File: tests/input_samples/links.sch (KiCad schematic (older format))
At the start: 4 parts, among them J1 Molex KK, J2 Molex KK

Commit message: Added `datasheet_as_link` example.
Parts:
- C1: manf# (none) -> C0805C102K5RACTU
- J1, J2: manf# (none) -> 0022232021
- R1: manf# (none) -> CR0805-JW-102ELF
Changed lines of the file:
@@
 F 3 "https://www.molex.com/webdocs/datasheets/pdf/en-us//0022232021_PCB_HEADERS.pdf" H 2850 2300 50  0001 C CNN
 F 4 "900-0022232021-ND" H 2850 2300 50  0001 C CNN "digikey#"
+F 5 "0022232021" H 2850 2300 50  0001 C CNN "manf#"
 	1    2850 2300
 	1    0    0    -1
@@
 F 3 "https://www.molex.com/webdocs/datasheets/pdf/en-us//0022232021_PCB_HEADERS.pdf" H 4500 2300 50  0001 C CNN
 F 4 "900-0022232021-ND" H 4500 2300 50  0001 C CNN "digikey#"
+F 5 "0022232021" H 4500 2300 50  0001 C CNN "manf#"
 	1    4500 2300
 	-1   0    0    -1
@@
 F 3 "https://www.bourns.com/docs/product-datasheets/CRxxxxx.pdf" H 3450 2300 50  0001 C CNN
 F 4 "CR0805-JW-102ELFCT-ND" V 3450 2300 50  0001 C CNN "digikey#"
+F 5 "CR0805-JW-102ELF" V 3450 2300 50  0001 C CNN "manf#"
 	1    3450 2300
 	0    1    1    0
@@
 F 3 "https://content.kemet.com/datasheets/KEM_C1002_X7R_SMD.pdf" H 3750 2500 50  0001 C CNN
 F 4 "399-1147-1-ND" H 3750 2500 50  0001 C CNN "digikey#"
+F 5 "C0805C102K5RACTU" H 3750 2500 50  0001 C CNN "manf#"
 	1    3750 2500
 	1    0    0    -1

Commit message: Added test for data_sheet_as_link in the DNF section.
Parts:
- C1: Config (none) -> DNF
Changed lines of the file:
@@
 F 4 "399-1147-1-ND" H 3750 2500 50  0001 C CNN "digikey#"
 F 5 "C0805C102K5RACTU" H 3750 2500 50  0001 C CNN "manf#"
+F 6 "DNF" H 3750 2500 50  0001 C CNN "Config"
 	1    3750 2500
 	1    0    0    -1

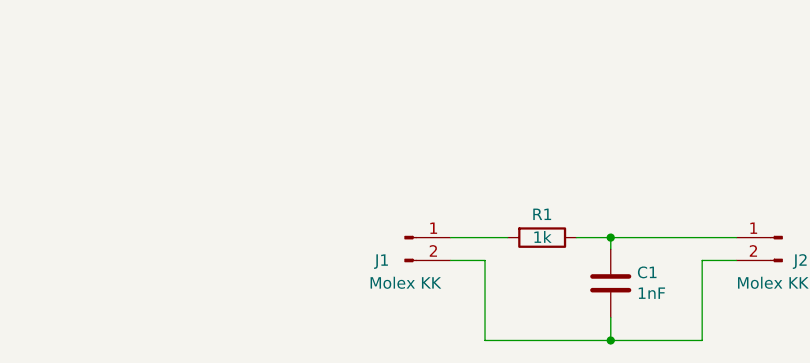
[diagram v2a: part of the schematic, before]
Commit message: Added UTF-8 text to a field.
Just to be sure it gets passed to XML output.
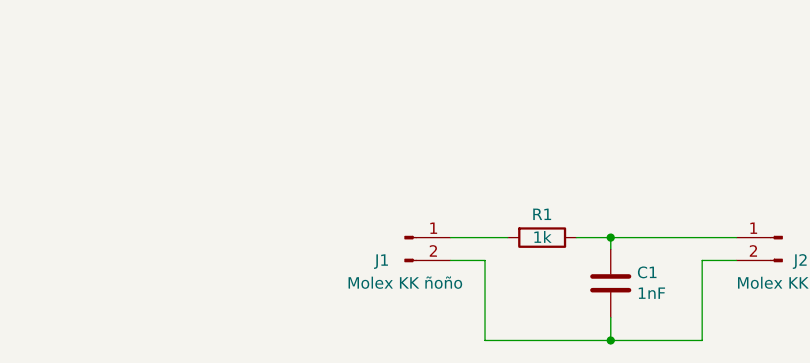
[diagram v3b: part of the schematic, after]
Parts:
- J1: value Molex KK -> Molex KK ñoño
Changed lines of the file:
@@
 P 2850 2300
 F 0 "J1" H 2750 2200 50  0000 C CNN
-F 1 "Molex KK" H 2850 2100 50  0000 C CNN
+F 1 "Molex KK ñoño" H 2850 2100 50  0000 C CNN
 F 2 "" H 2850 2300 50  0001 C CNN
 F 3 "https://www.molex.com/webdocs/datasheets/pdf/en-us//0022232021_PCB_HEADERS.pdf" H 2850 2300 50  0001 C CNN
